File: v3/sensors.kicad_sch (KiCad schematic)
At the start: 34 parts, among them IC1 SP721, J3 DIP8, J4 Conn_02x04_Counter_Clockwise

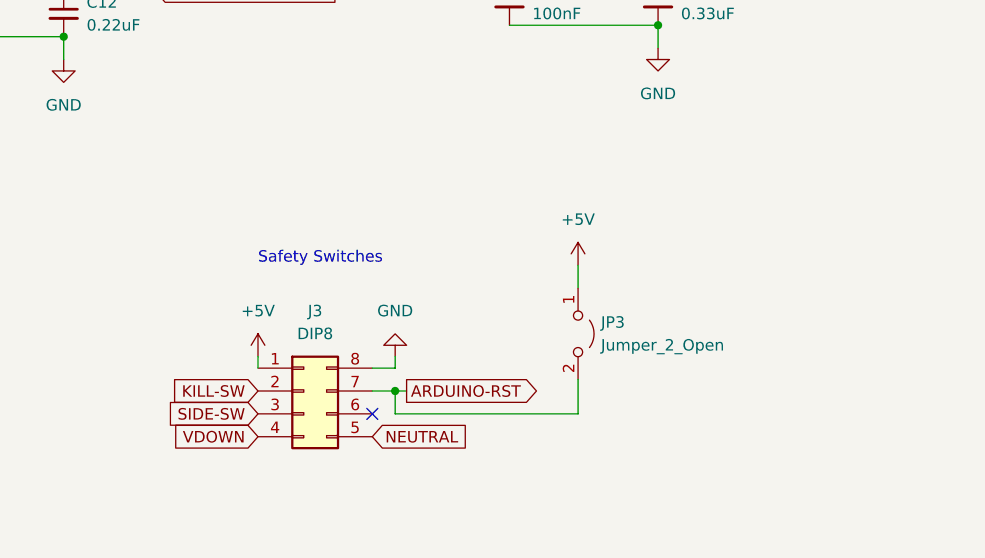
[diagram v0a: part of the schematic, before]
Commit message: change kill switch circuitry
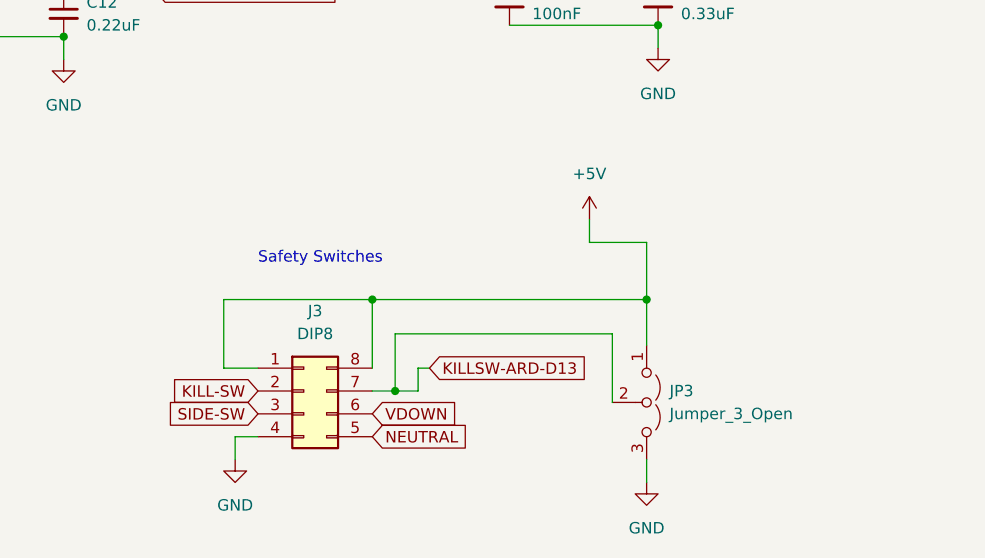
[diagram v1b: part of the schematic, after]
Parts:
- removed JP3: Jumper_2_Open, Jumper:SolderJumper-2_P1.3mm_Open_Pad1.0x1.5mm, symbol Jumper:Jumper_2_Open
- added JP3: Jumper_3_Open, Connector_PinHeader_2.54mm:PinHeader_1x03_P2.54mm_Vertical, symbol Jumper:Jumper_3_Open
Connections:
- net +5V: now also J3.8 (Pin_8), JP3.1 (A)
- net GND: now also J3.4 (Pin_4), JP3.3 (B); no longer J3.8 (Pin_8)
- net VDOWN: now also J3.6 (Pin_6); no longer J3.4 (Pin_4)
- net ARDUINO-RST renamed KILLSW-ARD-D13
- net KILLSW-ARD-D13: now also JP3.2 (C)
- no-connect marks 1 -> 0
